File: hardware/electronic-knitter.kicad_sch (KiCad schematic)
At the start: 37 parts, among them J101 SOLENOIDS, J102 ENC, J103 USB_C_Receptacle_USB2.0, J104 STLINK B2B, J105 Conn_ST_STDC14, Q101 AO3400A, SW101 BOOT, SW102 RESET, U101 STM32F103C8Tx, U102 SRV05-4, Y101 12MHz

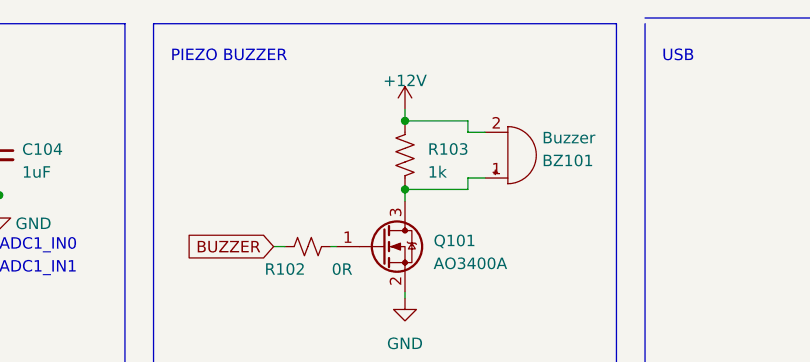
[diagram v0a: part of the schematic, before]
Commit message: fix project with stm32pio
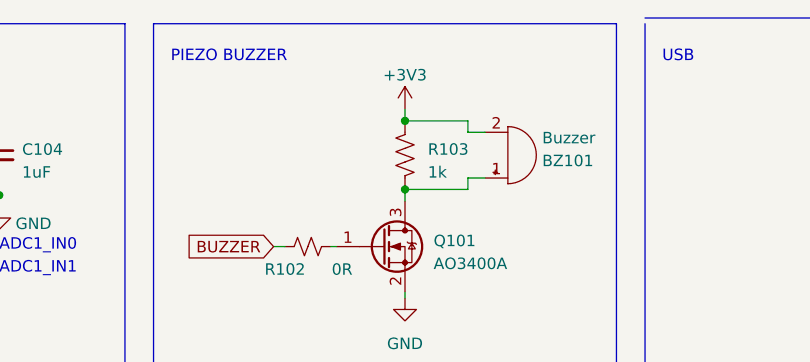
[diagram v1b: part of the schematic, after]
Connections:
- net +12V is gone; now on net +3V3: BZ101.2 (+), R103.1
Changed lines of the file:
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@@
-    )
-  )
-  (symbol (lib_id "power:+12V") (at 140.335 25.4 0) (unit 1)
-    (in_bom yes) (on_board yes) (dnp no) (fields_autoplaced)
-    (property "Reference" "#PWR0108" (at 140.335 29.21 0)
-      (effects (font (size 1.27 1.27)) hide)
-    )
-    (property "Value" "+12V" (at 140.335 22.225 0)
-      (effects (font (size 1.27 1.27)))
-    )
-    (property "Footprint" "" (at 140.335 25.4 0)
-      (effects (font (size 1.27 1.27)) hide)
-    )
-    (property "Datasheet" "" (at 140.335 25.4 0)
-      (effects (font (size 1.27 1.27)) hide)
-    )
-    (pin "1")
-    (instances
-      (project "electronic-knitter"
-        (path "/a3f4eded-ecb9-44ce-82ad-ad815e00f2c9"
-          (reference "#PWR0108") (unit 1)
-        )
-      )
     )
   )
@@
         )
       )
+    )
+  )
+  (symbol (lib_id "power:+3V3") (at 140.335 25.4 0) (unit 1)
+    (in_bom yes) (on_board yes) (dnp no) (fields_autoplaced)
+    (property "Reference" "#PWR0108" (at 140.335 29.21 0)
+      (effects (font (size 1.27 1.27)) hide)
+    )
+    (property "Value" "+3V3" (at 140.335 21.59 0)
+      (effects (font (size 1.27 1.27)))
+    )
+    (property "Footprint" "" (at 140.335 25.4 0)
+      (effects (font (size 1.27 1.27)) hide)
+    )
+    (property "Datasheet" "" (at 140.335 25.4 0)
+      (effects (font (size 1.27 1.27)) hide)
+    )
+    (pin "1")
+    (instances
+      (project "electronic-knitter"
+        (path "/a3f4eded-ecb9-44ce-82ad-ad815e00f2c9"
+          (reference "#PWR0108") (unit 1)
+        )
+      )

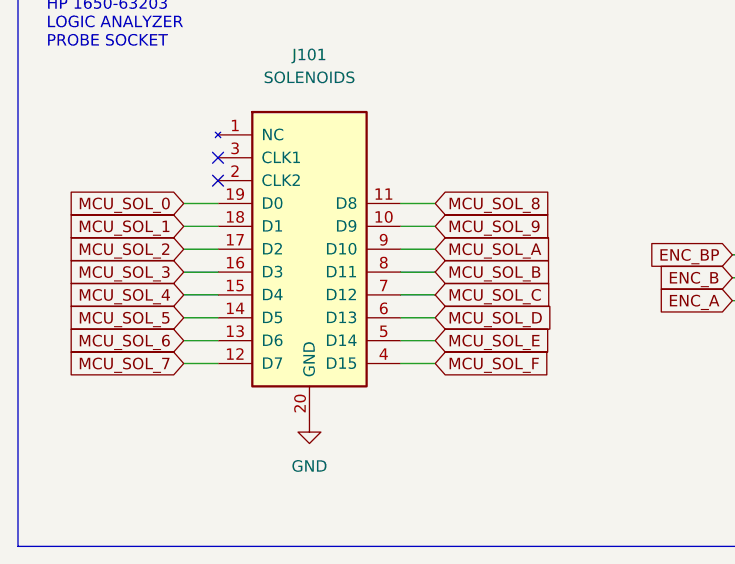
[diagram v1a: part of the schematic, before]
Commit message: work on firmware and swap solenoid banks to match actual pinout
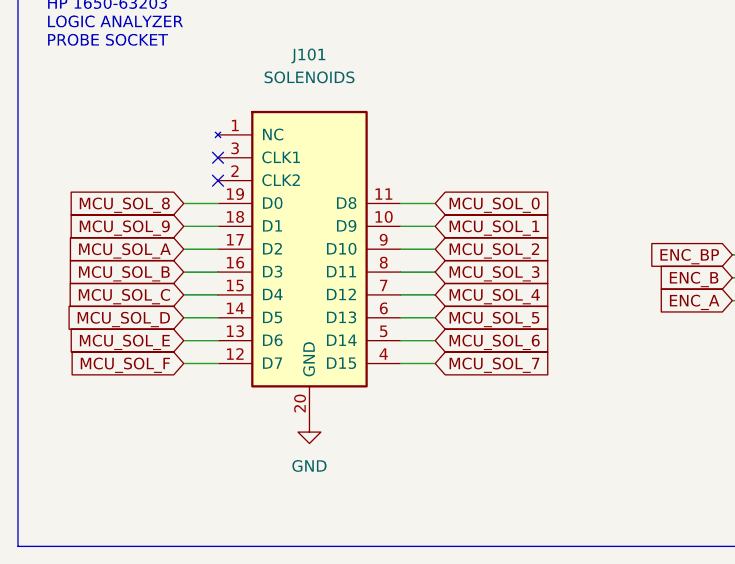
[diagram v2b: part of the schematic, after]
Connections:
- net MCU_SOL_0: now also J101.11 (D8); no longer J101.19 (D0)
- net MCU_SOL_1: now also J101.10 (D9); no longer J101.18 (D1)
- net MCU_SOL_2: now also J101.9 (D10); no longer J101.17 (D2)
- net MCU_SOL_3: now also J101.8 (D11); no longer J101.16 (D3)
- net MCU_SOL_4: now also J101.7 (D12); no longer J101.15 (D4)
- net MCU_SOL_5: now also J101.6 (D13); no longer J101.14 (D5)
- net MCU_SOL_6: now also J101.5 (D14); no longer J101.13 (D6)
- net MCU_SOL_7: now also J101.4 (D15); no longer J101.12 (D7)
- net MCU_SOL_8: now also J101.19 (D0); no longer J101.11 (D8)
- net MCU_SOL_9: now also J101.18 (D1); no longer J101.10 (D9)
- net MCU_SOL_A: now also J101.17 (D2); no longer J101.9 (D10)
- net MCU_SOL_B: now also J101.16 (D3); no longer J101.8 (D11)
- net MCU_SOL_C: now also J101.15 (D4); no longer J101.7 (D12)
- net MCU_SOL_D: now also J101.14 (D5); no longer J101.6 (D13)
- net MCU_SOL_E: now also J101.13 (D6); no longer J101.5 (D14)
- net MCU_SOL_F: now also J101.12 (D7); no longer J101.4 (D15)
